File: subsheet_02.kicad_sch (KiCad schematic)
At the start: 0 parts

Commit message: schematic : place U1 and U2, the CPLD and the Gate array connector
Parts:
- added U2: GATE_ARRAY_MO5_V1_SOCKET, Package_LCC:PLCC-68_THT-Socket, symbol gate_array_v1:GATE_ARRAY_MO5_V1_SOCKET
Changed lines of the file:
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@@
     (comment 4 "Original repository : https://github.com/sporniket/...")
   )
+  (symbol (lib_id "gate_array_v1:GATE_ARRAY_MO5_V1_SOCKET") (at 105.41 132.08 0) (unit 1)
+    (in_bom yes) (on_board yes) (dnp no)
+    (property "Reference" "U2" (at 124.46 91.44 0)
+      (effects (font (size 1.27 1.27)) (justify left top))
+    )
+    (property "Value" "GATE_ARRAY_MO5_V1_SOCKET" (at 124.46 93.98 0)
+      (effects (font (size 1.27 1.27) bold) (justify left top))
+    )
+    (property "Footprint" "Package_LCC:PLCC-68_THT-Socket" (at 124.46 88.9 0)
+      (effects (font (size 1.27 1.27)) (justify left top) hide)
+    )
+    (property "Datasheet" "" (at 105.41 132.08 0)
+      (effects (font (size 1.27 1.27)) hide)
+    )
+    (pin "52")
+    (pin "60")
+    (pin "46")
+    (pin "65")
+    (pin "42")
+    (pin "37")
+    (pin "61")
+    (pin "64")
+    (pin "54")
+    (pin "9")
+    (pin "66")
+    (pin "47")
+    (pin "44")
+    (pin "48")
+    (pin "53")
+    (pin "40")
+    (pin "31")
+    (pin "50")
+    (pin "39")
+    (pin "12")
+    (pin "1")
+    (pin "15")
+    (pin "14")
+    (pin "11")
+    (pin "13")
+    (pin "10")
+    (pin "29")
+    (pin "28")
+    (pin "22")
+    (pin "20")
+    (pin "18")
+    (pin "17")
+    (pin "23")
+    (pin "19")
+    (pin "2")
+    (pin "21")
+    (pin "3")
+    (pin "16")
+    (pin "7")
+    (pin "43")
+    (pin "67")
+    (pin "57")
+    (pin "25")
+    (pin "45")
+    (pin "5")
+    (pin "32")
+    (pin "58")
+    (pin "30")
+    (pin "41")
+    (pin "33")
+    (pin "4")
+    (pin "27")
+    (pin "55")
+    (pin "59")
+    (pin "35")
+    (pin "62")
+    (pin "26")
+    (pin "68")
+    (pin "51")
+    (pin "36")
+    (pin "24")
+    (pin "56")
+    (pin "6")
+    (pin "38")
+    (pin "49")
+    (pin "34")
+    (pin "63")
+    (pin "8")
+    (instances
+      (project "mo5-ga-motorola-repl--atf1508"
+        (path "/04881907-557f-4bbf-81fb-63c3424a1f56/2f3e2774-89af-48f0-a289-d0988ad66b48"
+          (reference "U2") (unit 1)
+        )
+      )
+    )
+  )
 )

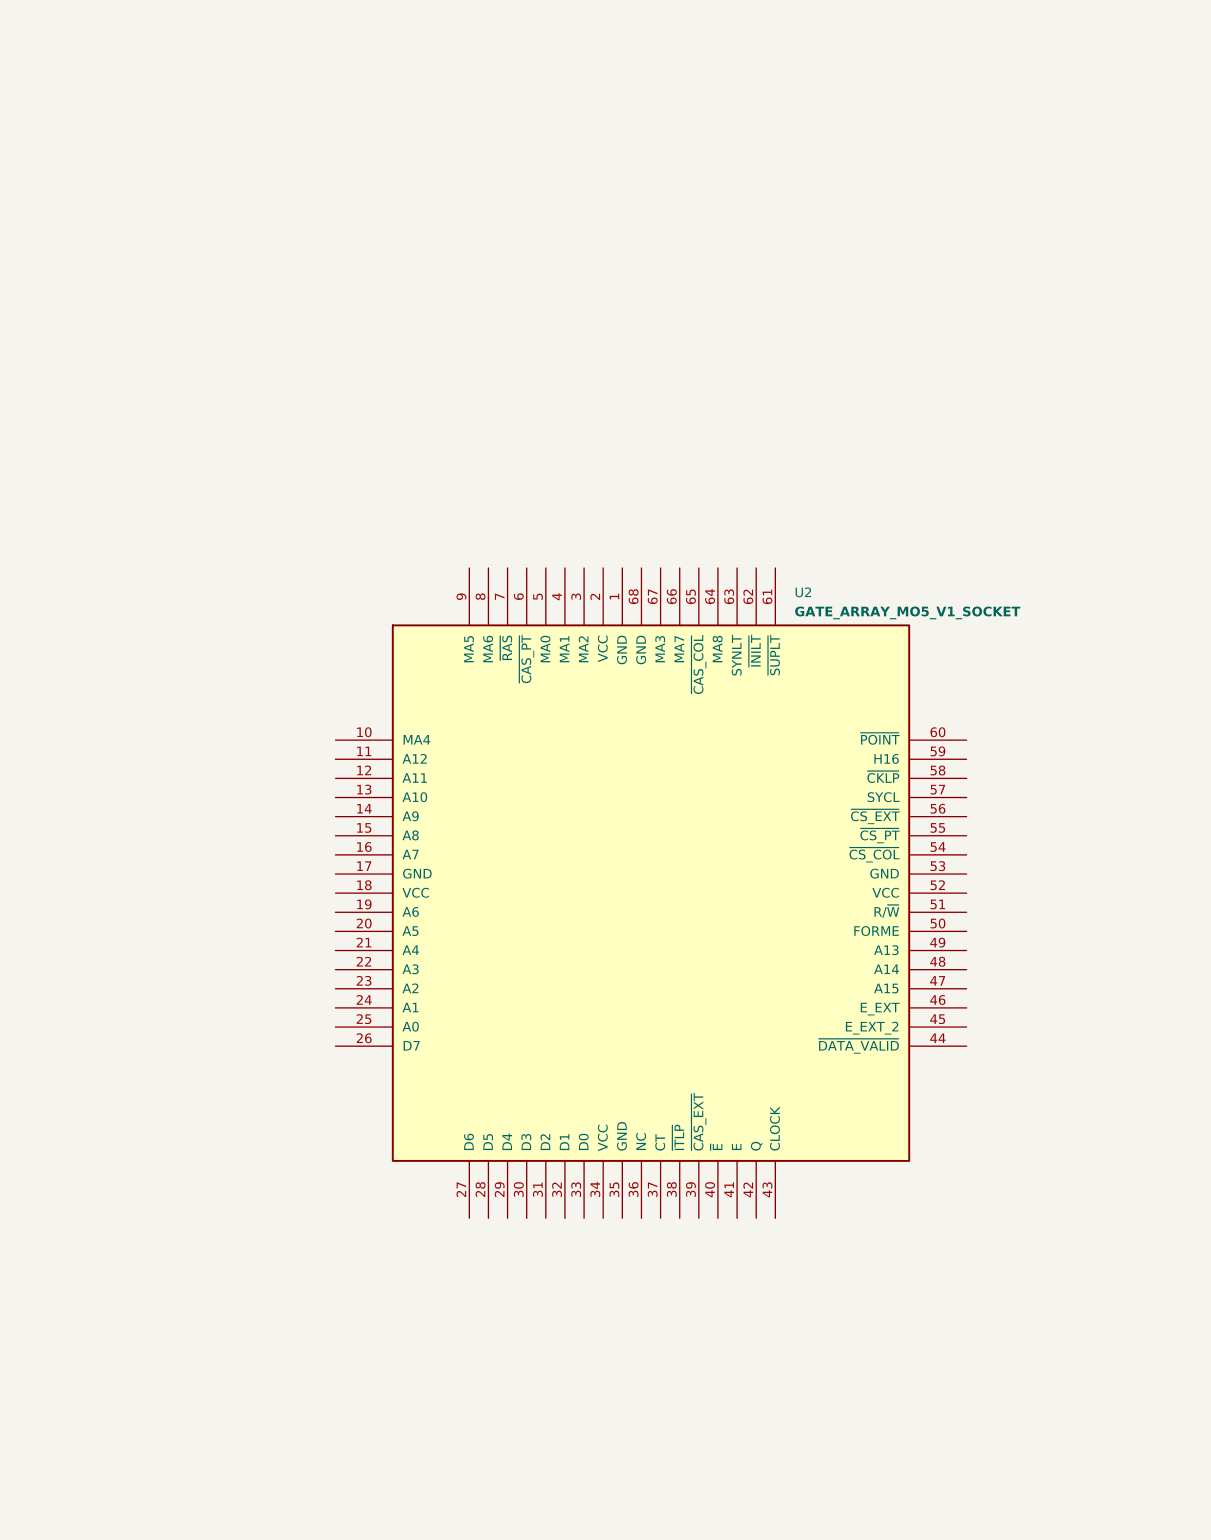
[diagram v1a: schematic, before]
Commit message: schematic : setup all signals going through U2
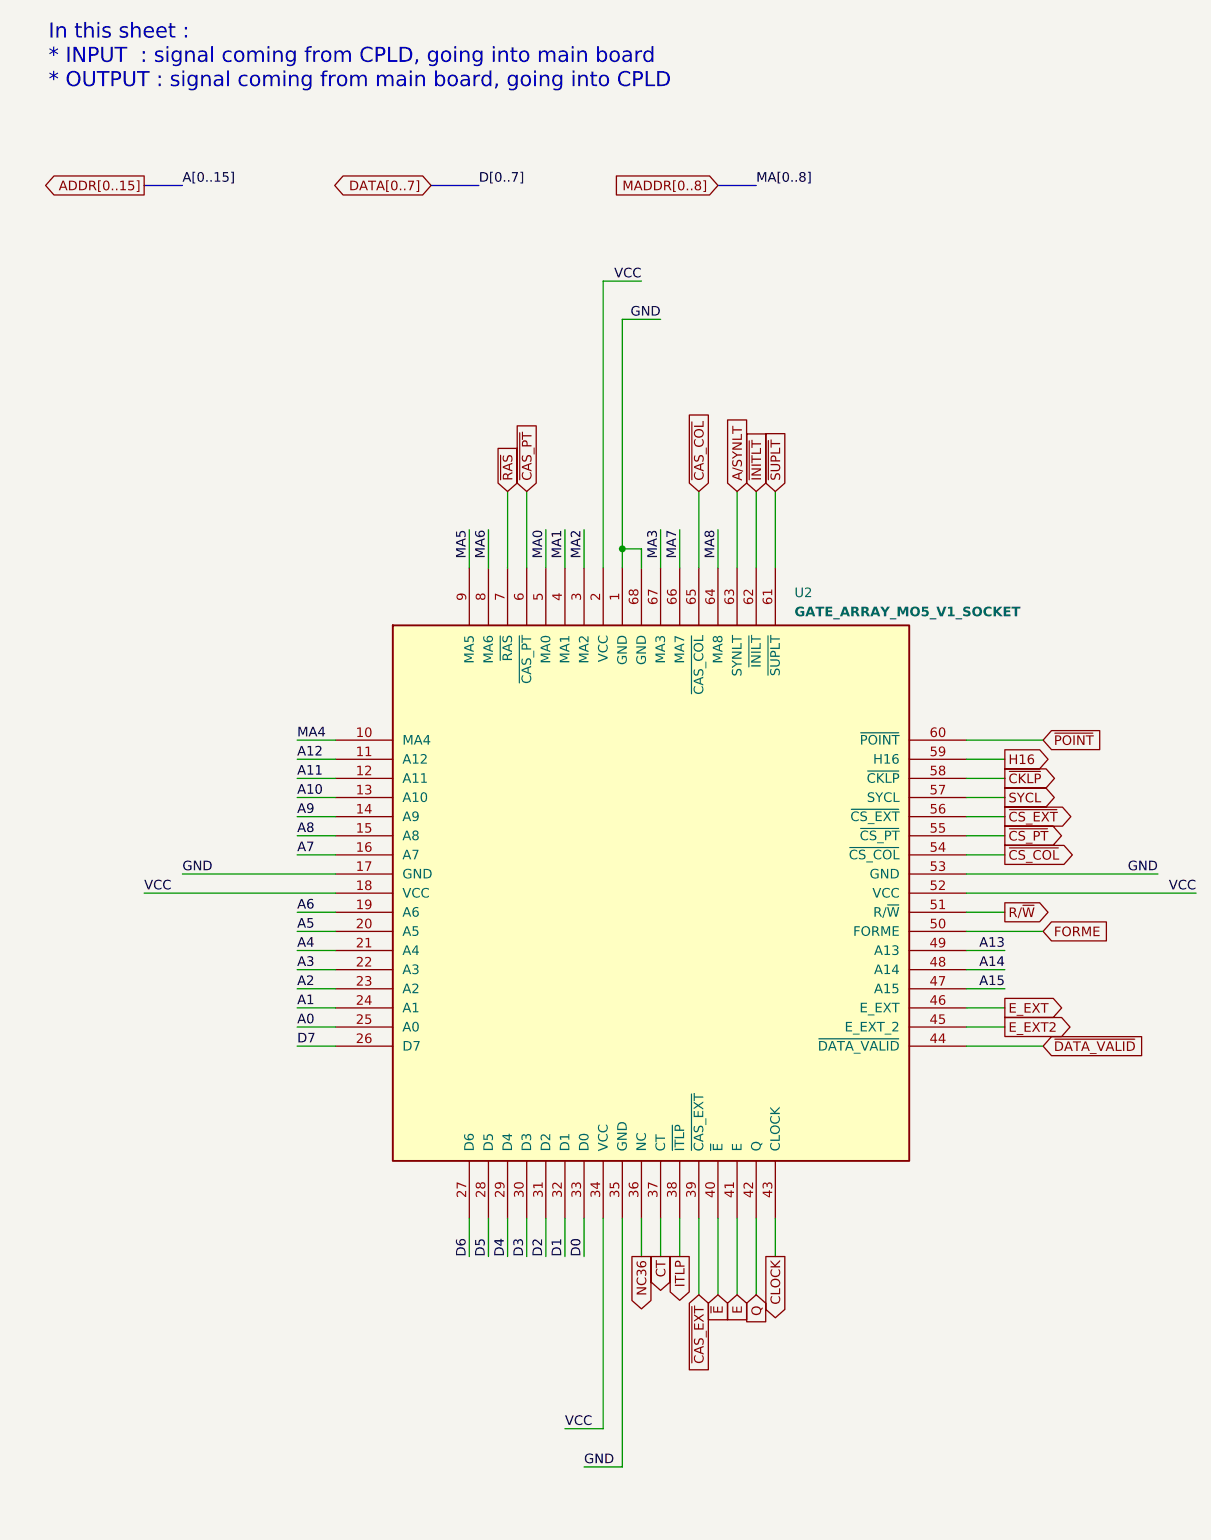
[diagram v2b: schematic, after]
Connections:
- net GND: now reaches U2.1 (GND)
- net GND: now also U2.17 (GND), U2.35 (GND), U2.53 (GND), U2.68 (GND)
- net MA4: now reaches U2.10 (MA4)
- net A12: now reaches U2.11 (A12)
- net A11: now reaches U2.12 (A11)
- net A10: now reaches U2.13 (A10)
- net A9: now reaches U2.14 (A9)
- net A8: now reaches U2.15 (A8)
- net A7: now reaches U2.16 (A7)
- net VCC: now reaches U2.18 (VCC)
- net VCC: now also U2.2 (VCC), U2.34 (VCC), U2.52 (VCC)
- net A6: now reaches U2.19 (A6)
- net A5: now reaches U2.20 (A5)
- net A4: now reaches U2.21 (A4)
- net A3: now reaches U2.22 (A3)
- net A2: now reaches U2.23 (A2)
- net A1: now reaches U2.24 (A1)
- net A0: now reaches U2.25 (A0)
- net D7: now reaches U2.26 (D7)
- net D6: now reaches U2.27 (D6)
- net D5: now reaches U2.28 (D5)
- net D4: now reaches U2.29 (D4)
- net MA2: now reaches U2.3 (MA2)
- net D3: now reaches U2.30 (D3)
- net D2: now reaches U2.31 (D2)
- net D1: now reaches U2.32 (D1)
- net D0: now reaches U2.33 (D0)
- net NC36: now reaches U2.36 (NC)
- net CT: now reaches U2.37 (CT)
- net ITLP: now reaches U2.38 (~{ITLP})
- net ~{CAS_EXT}: now reaches U2.39 (~{CAS_EXT})
- net MA1: now reaches U2.4 (MA1)
- net ~{E}: now reaches U2.40 (~{E})
- net E: now reaches U2.41 (E)
- net Q: now reaches U2.42 (Q)
- net CLOCK: now reaches U2.43 (CLOCK)
- net ~{DATA_VALID}: now reaches U2.44 (~{DATA_VALID})
- net E_EXT2: now reaches U2.45 (E_EXT_2)
- net E_EXT: now reaches U2.46 (E_EXT)
- net A15: now reaches U2.47 (A15)
- net A14: now reaches U2.48 (A14)
- net A13: now reaches U2.49 (A13)
- net MA0: now reaches U2.5 (MA0)
- net FORME: now reaches U2.50 (FORME)
- net R/~{W}: now reaches U2.51 (R/~{W})
- net ~{CS_COL}: now reaches U2.54 (~{CS_COL})
- net ~{CS_PT}: now reaches U2.55 (~{CS_PT})
- net ~{CS_EXT}: now reaches U2.56 (~{CS_EXT})
- net SYCL: now reaches U2.57 (SYCL)
- net ~{CKLP}: now reaches U2.58 (~{CKLP})
- net H16: now reaches U2.59 (H16)
- net ~{CAS_PT}: now reaches U2.6 (~{CAS_PT})
- net ~{POINT}: now reaches U2.60 (~{POINT})
- net ~{SUPLT}: now reaches U2.61 (~{SUPLT})
- net ~{INITLT}: now reaches U2.62 (~{INILT})
- net A/SYNLT: now reaches U2.63 (SYNLT)
- net MA8: now reaches U2.64 (MA8)
- net ~{CAS_COL}: now reaches U2.65 (~{CAS_COL})
- net MA7: now reaches U2.66 (MA7)
- net MA3: now reaches U2.67 (MA3)
- net ~{RAS}: now reaches U2.7 (~{RAS})
- net MA6: now reaches U2.8 (MA6)
- net MA5: now reaches U2.9 (MA5)
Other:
- note added: "In this sheet : * INPUT : signal coming from CPLD, going into main board * OUTPUT : signal coming from main board, going into CPLD"

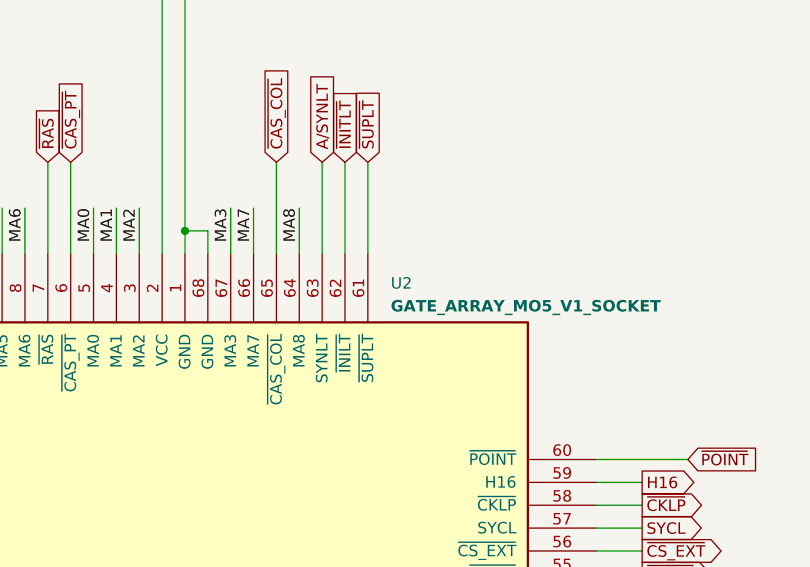
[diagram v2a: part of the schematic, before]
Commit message: schematic : U2 renamed to J2
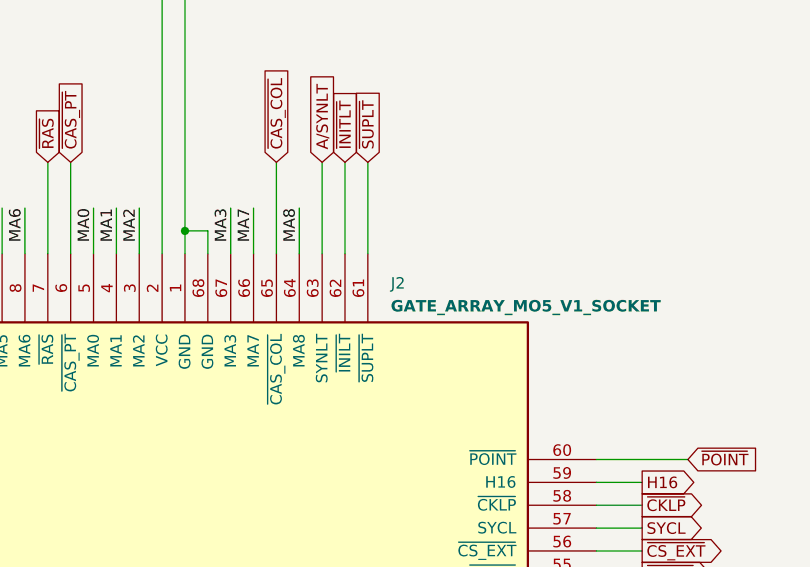
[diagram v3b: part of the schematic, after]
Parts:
- renumbered U2 to J2
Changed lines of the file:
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@@
   (symbol (lib_id "gate_array_v1:GATE_ARRAY_MO5_V1_SOCKET") (at 105.41 132.08 0) (unit 1)
     (in_bom yes) (on_board yes) (dnp no)
-    (property "Reference" "U2" (at 124.46 91.44 0)
+    (property "Reference" "J2" (at 124.46 91.44 0)
       (effects (font (size 1.27 1.27)) (justify left top))
     )
@@
       (project "mo5-ga-motorola-repl--atf1508"
         (path "/04881907-557f-4bbf-81fb-63c3424a1f56/2f3e2774-89af-48f0-a289-d0988ad66b48"
-          (reference "U2") (unit 1)
+          (reference "J2") (unit 1)
         )
       )
